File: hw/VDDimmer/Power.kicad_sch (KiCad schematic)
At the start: 37 parts, among them J2 VIN 9-24V, Q5 SUD50P06-15, U2 AP64350SP-13, U3 AMS1117-3.3

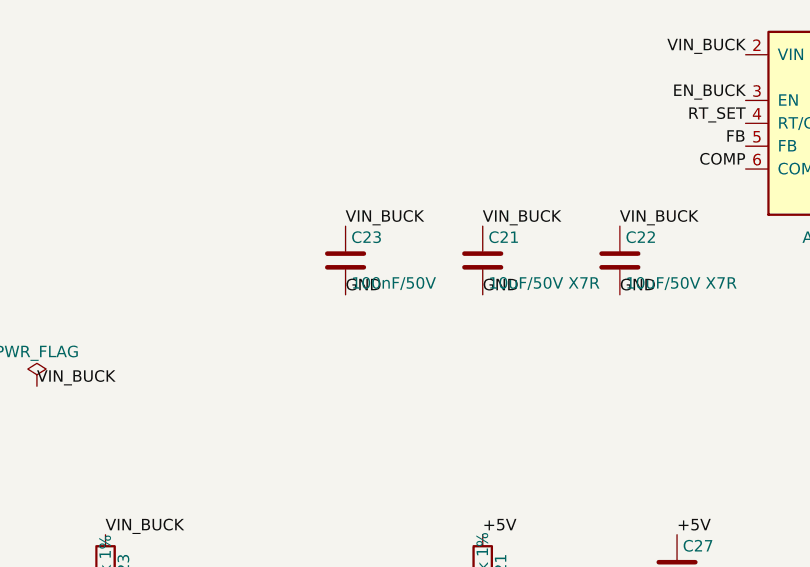
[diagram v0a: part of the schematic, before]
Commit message: Route input protection chain and VIN_BUCK distribution
C23 -> 0402 (100nF/25V): hot loop 14.31 -> 13.31 mm2, 11% margin.
VIN corridor necked to 0.6mm to hold clearance to the GND return.

Routed: VIN_RAW (J2->F1), VIN_FUSED (F1->D5->Q5 tab, routed above D5
to clear its GND pad), QREV_G (Q5 gate -> R20 -> D6), VIN_BUCK
distribution (R30/L3 -> C21/C22 -> R31 -> R23 -> buck), VIN_DAMP.

0 real DRC errors. 24-28 reported errors are C23's 4 phantom pads,
re-injected by update_pcb_from_schematic; place_component does not
have this bug but produces footprints with no schematic identity,
so it cannot carry nets.

Co-Authored-By: Claude Opus 5 (1M context) <noreply@anthropic.com>
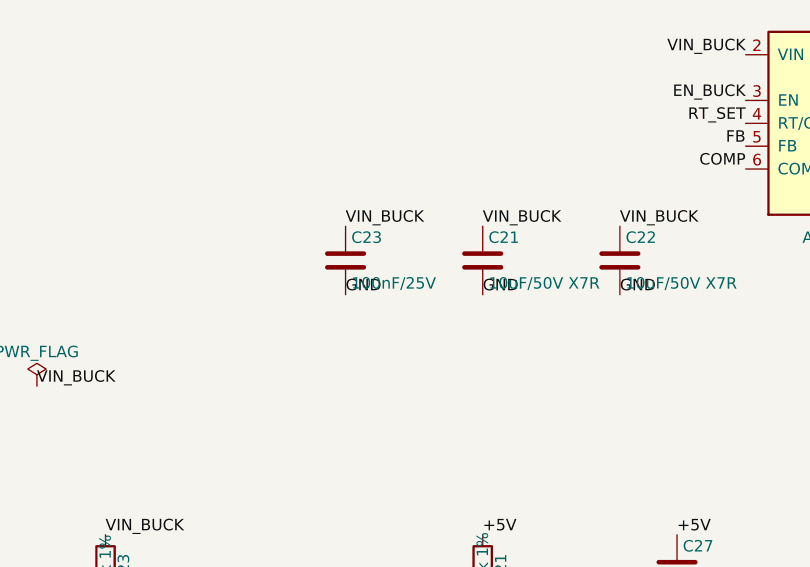
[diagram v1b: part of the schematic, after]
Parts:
- C23: value 100nF/50V -> 100nF/25V; footprint Capacitor_SMD:C_0603_1608Metric -> Capacitor_SMD:C_0402_1005Metric
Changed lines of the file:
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@@
 			)
 		)
-		(property "Value" "100nF/50V"
+		(property "Value" "100nF/25V"
 			(at 135.255 107.95 0)
 			(effects
@@
 			)
 		)
-		(property "Footprint" "Capacitor_SMD:C_0603_1608Metric"
+		(property "Footprint" "Capacitor_SMD:C_0402_1005Metric"
 			(at 134.62 105.41 0)
 			(hide yes)

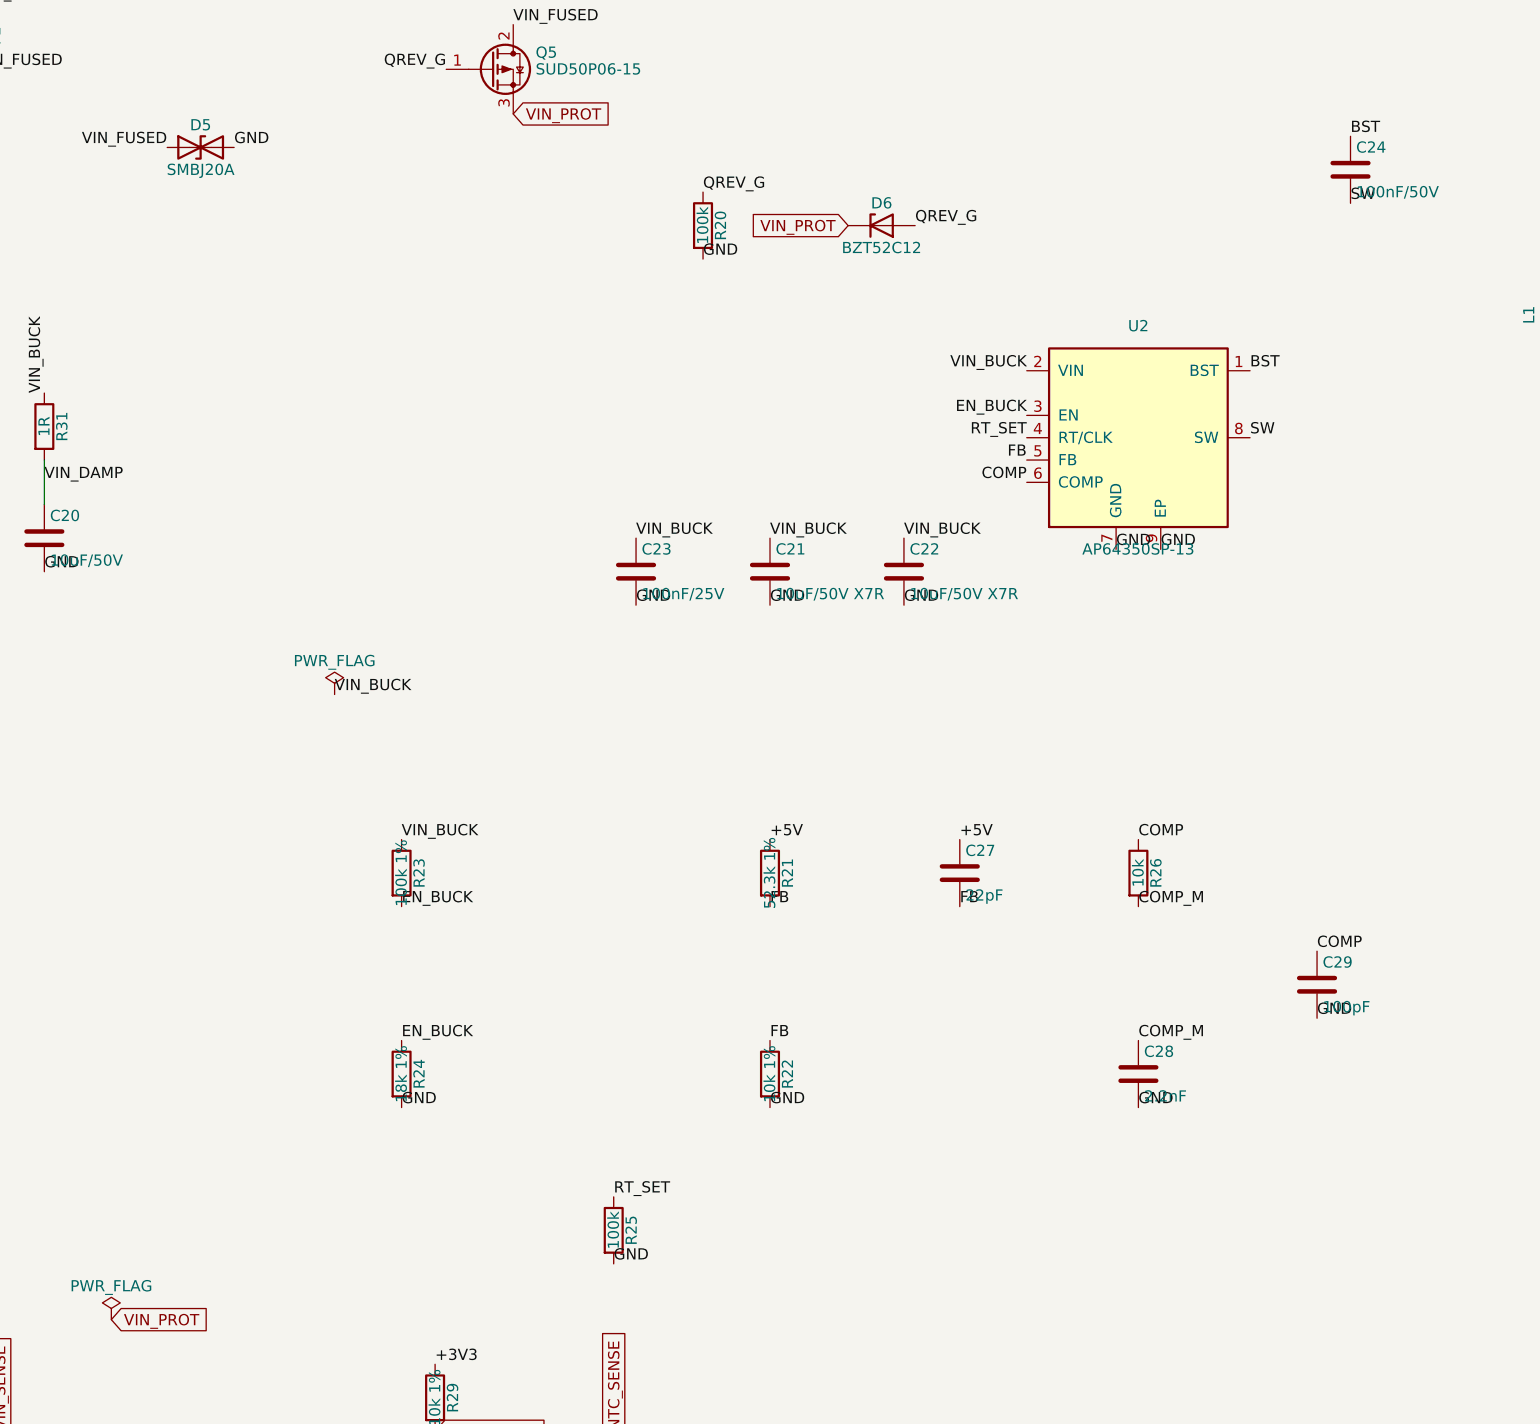
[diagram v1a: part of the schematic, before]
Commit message: Swap buck to AP63301WU-7: hot loop 13.31 -> 4.60 mm2
The AP64350's SO-8EP pinout (VIN pin2 / GND pin7 diagonal, BST and SW
between them) has no valid 2-layer routing: Cin above the IC forces a
VIN/BST crossing, Cin below encloses EN and RT with no escape that
doesn't either break the 8.5.3 keepout or push the hot loop to
16.5 mm2. Measured, not estimated.

AP63301WU-7 (C2158003, TSOT-23-6, 3.8-32V, 3A, 500kHz, spread
spectrum) has VIN (pin3) and GND (pin4) adjacent on the bottom edge.
Cin bridges them directly from below:

  hot loop  4.60 mm2  (target <15, 69% margin)
  vias in loop 0
  BST cap bridges pin6/pin5, adjacent on the right edge
  FB and EN on the free left edge, nothing enclosing them

Internally compensated at fixed 500kHz, so R25 (RT_SET), R26/C28
(COMP network) and C29 are deleted - 4 fewer parts and 3 fewer nets.
500kHz unchanged so L1 stays 10uH and C25/C26 unchanged. FB divider
unchanged: 52.3k/10k with 0.8V ref = 4.98V.

D5 SMBJ20A -> SMBJ18A (C19077573, Preferred, 42k stock): 29.2V clamp
sits under the AP63301's 32V abs max; SMBJ20A's 32.4V did not.

New symbol VANDIMMER:AP63301 authored. ERC 0/0, DRC 0 real errors.
Remaining 540 DRC errors are 24 Konnect phantom pads on U2 and C23.

Co-Authored-By: Claude Opus 5 (1M context) <noreply@anthropic.com>
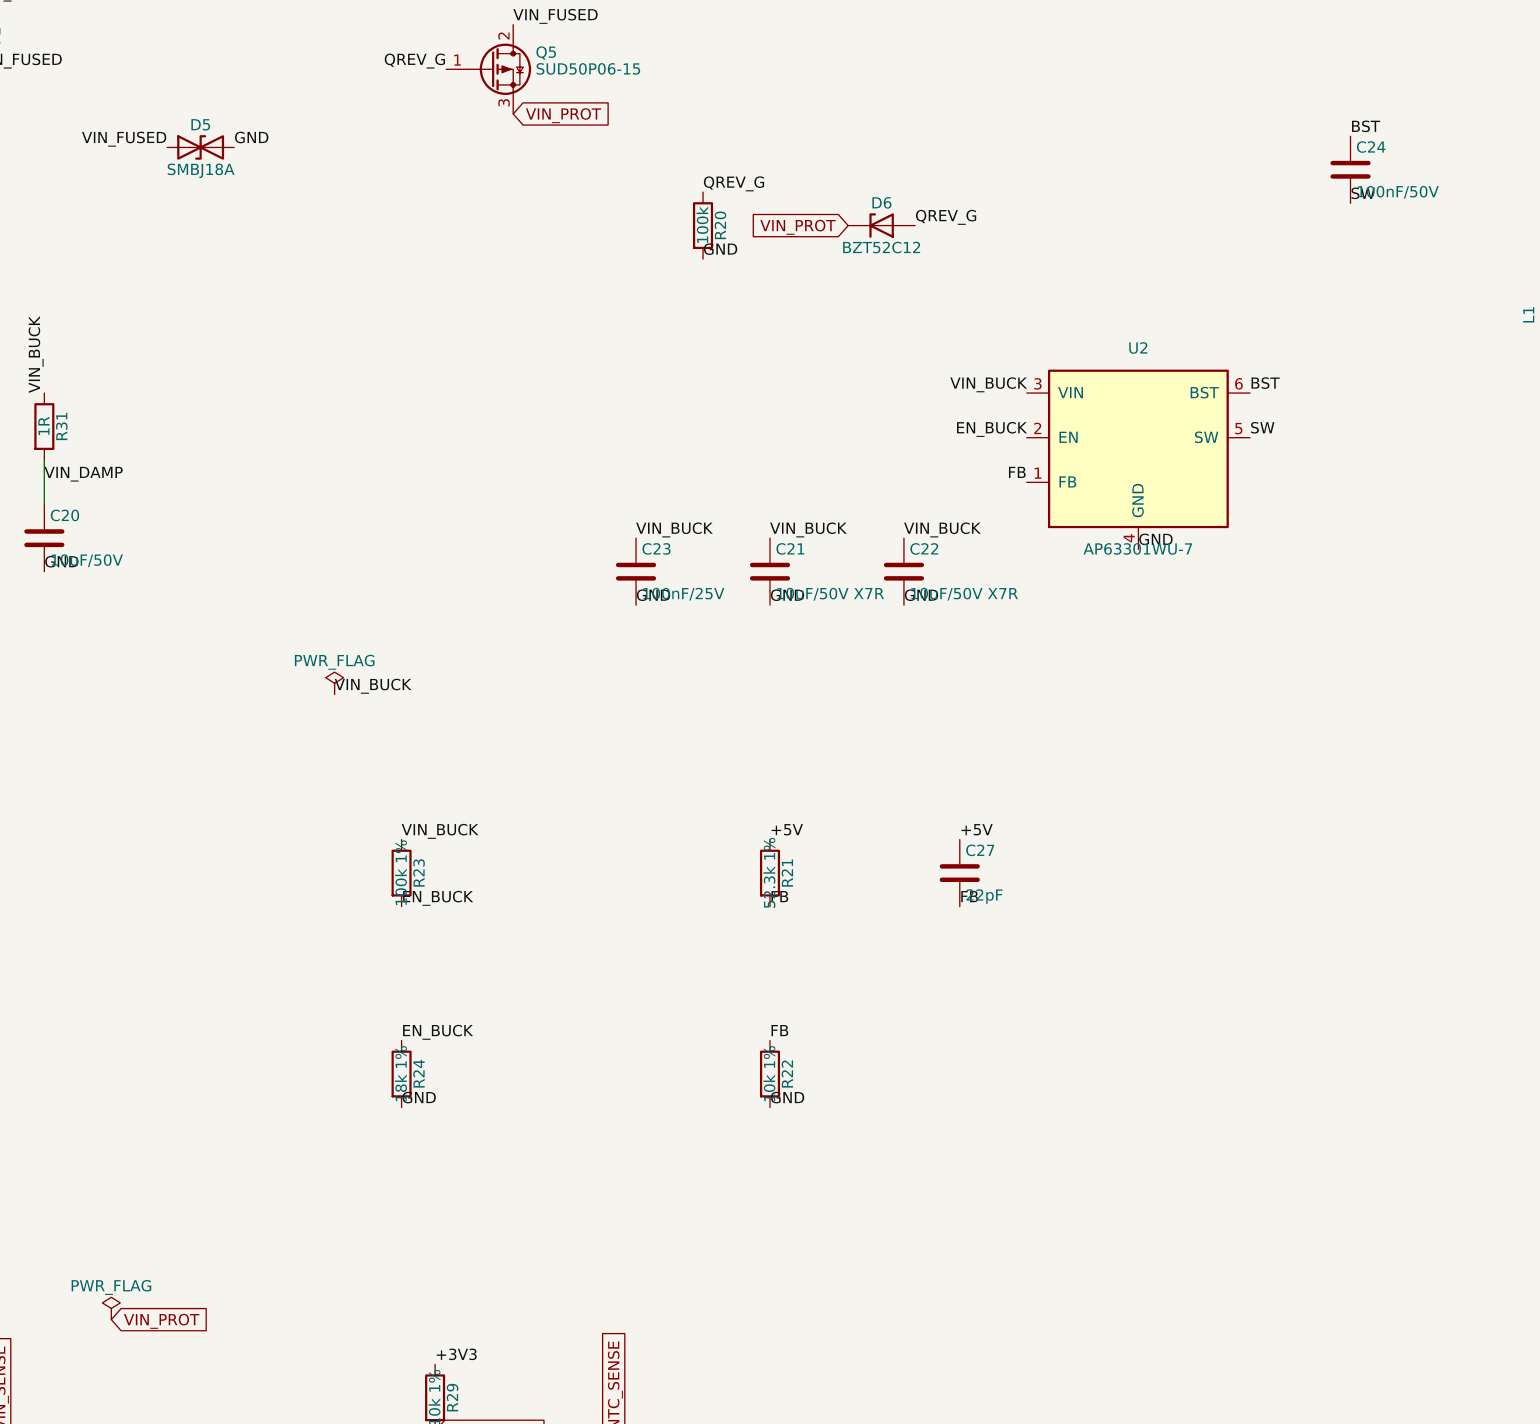
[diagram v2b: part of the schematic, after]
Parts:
- removed C28: 2.2nF, Capacitor_SMD:C_0603_1608Metric, symbol Device:C
- removed C29: 100pF, Capacitor_SMD:C_0603_1608Metric, symbol Device:C
- removed R25: 100k, Resistor_SMD:R_0805_2012Metric, symbol Device:R
- removed R26: 10k, Resistor_SMD:R_0805_2012Metric, symbol Device:R
- removed U2: AP64350SP-13, Package_SO:SOIC-8-1EP_3.9x4.9mm_P1.27mm_EP2.41x3.3mm_ThermalVias, symbol VANDIMMER:AP64350
- added U2: AP63301WU-7, Package_TO_SOT_SMD:TSOT-23-6, symbol VANDIMMER:AP63301
- D5: value SMBJ20A -> SMBJ18A
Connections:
- net BST: now also U2.6 (BST)
- net EN_BUCK: now also U2.2 (EN)
- net FB: now also U2.1 (FB)
- net GND: now also U2.4 (GND)
- net SW: now also U2.5 (SW)
- net VIN_BUCK: now also U2.3 (VIN)

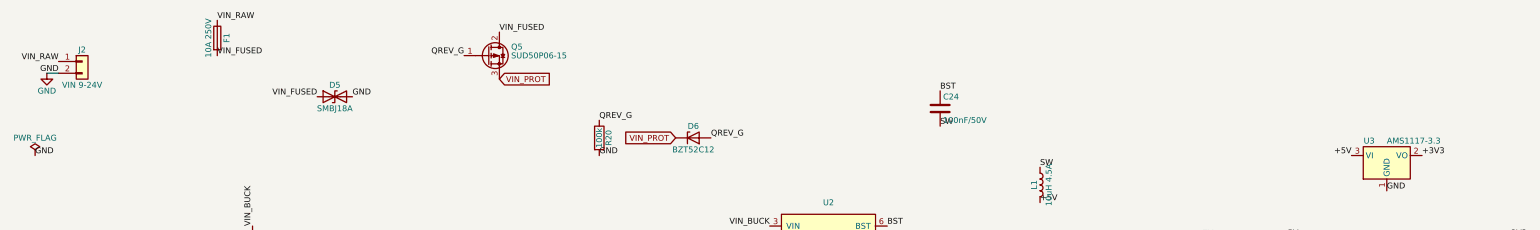
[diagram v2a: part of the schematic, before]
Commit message: Schematic pass: MPN/LCSC/Manufacturer on all 79 sourced parts
F1 -> "8A 250V", U3 -> "BL1117-33CX", J2 -> "VIN 12V" (was "VIN 9-24V",
which invited 24 V into an 18 V TVS). R11/R12 values cleaned to "47R" with
the DNP intent moved into the Assembly field. ERC still 0 violations.

Every sourced part now carries MPN, LCSC and Manufacturer, plus an Assembly
note anywhere the choice needs explaining - why D5 is an SMBJ18A, why R30's
current rating still needs checking, why L1 is candidate-only.

Two things this pass could NOT do, both because no MCP tool writes them:

- KiCad's (dnp yes) attribute. R11 and R12 must be flagged in the GUI; their
  Assembly fields say so. All five text-only DNPs were in this state, but
  L3/C20/R31 are now fitted by decision, so only R11/R12 remain.
- Fields on units 2-5 of a multi-unit symbol. Konnect writes unit 1 only,
  where the GUI propagates to all units. U4/U5 are 5-unit 74HCT125s, so
  grouping a BOM by MPN splits U5 into two lines and would order 3 of a
  2-off part. tools/export-bom.sh groups by Value+Footprint instead, which
  collapses correctly - 49 lines, 96 parts, and the 15 lines without an LCSC
  are exactly the mounting holes and hand-fit connectors.

Also checked and left alone: the U4/U5 symbol's lib_id is 74AHCT125 while its
value is 74HCT125. AHCT would be the conventional WS2812 level shifter, but
JLC has 70 of it in SO-14 against 88,003 of the HCT part, and HCT is fine here
- TTL inputs, 15 ns against 300 ns bit times. The value is the buyable intent.

Co-Authored-By: Claude Opus 5 (1M context) <noreply@anthropic.com>
Claude-Session: https://claude.ai/code/session_01QsYnM2qRBWQsyKPH1v7rLR
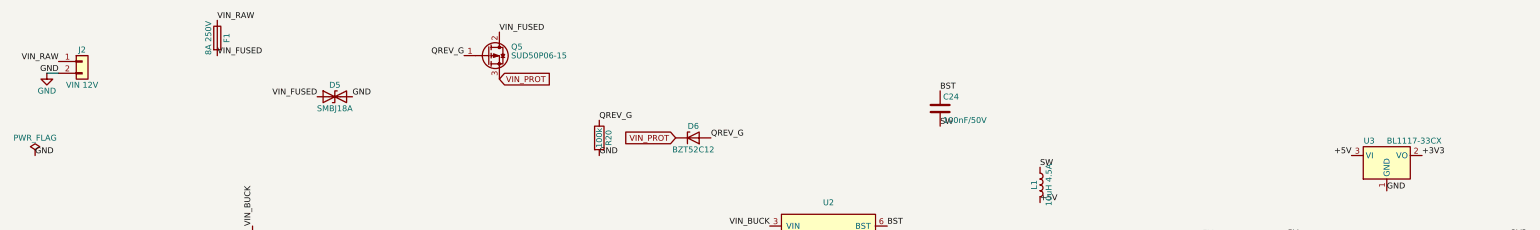
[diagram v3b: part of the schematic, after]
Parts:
- C20: Assembly DNP - spare input cap, populate with L3 -> LC filter cap - NOW FITTED per the 2026-08-29 decision, no 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; LCSC (none) -> C5156756; MPN (none) -> FS32X106K101EGG; Manufacturer (none) -> PSA
- C21, C22: LCSC (none) -> C5156756; MPN (none) -> FS32X106K101EGG; Manufacturer (none) -> PSA
- C23: Assembly (none) -> buck Cin - keep the 2.51 mm2 hot loop; do not relocate; LCSC (none) -> C307331; MPN (none) -> CL05B104KB54PNC; Manufacturer (none) -> Samsung Electro-Mechanics
- C24, C32, C33, C34: LCSC (none) -> C14663; MPN (none) -> CC0603KRX7R9BB104; Manufacturer (none) -> YAGEO
- C25, C26, C31: LCSC (none) -> C12891; MPN (none) -> CL31A226KAHNNNE; Manufacturer (none) -> Samsung Electro-Mechanics
- C27: LCSC (none) -> C1653; MPN (none) -> CL10C220JB8NNNC; Manufacturer (none) -> Samsung Electro-Mechanics
- C30: LCSC (none) -> C15850; MPN (none) -> CL21A106KAYNNNE; Manufacturer (none) -> Samsung Electro-Mechanics
- D5: Assembly (none) -> 18 V standoff, 29.2 V clamp - under U2's 32 V abs max. The 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; LCSC (none) -> C19077573; MPN (none) -> SMBJ18A; Manufacturer (none) -> hongjiacheng
- D6: LCSC (none) -> C19077410; MPN (none) -> BZT52C12; Manufacturer (none) -> hongjiacheng
- F1: value 10A 250V -> 8A 250V; Assembly (none) -> 8 A fuse - sized for the 5 A board cap with 25% continuous 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; LCSC (none) -> C54824501; MPN (none) -> LTC2410-1800TSK; Manufacturer (none) -> LUTE
- J2: value VIN 9-24V -> VIN 12V; Assembly (none) -> hand-fit. 12 V ONLY - D5 is an SMBJ18A (18 V standoff); 24 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; MPN (none) -> MC 1,5/2-G-5.08; Manufacturer (none) -> Phoenix Contact
- L1: Assembly (none) -> CANDIDATE ONLY - verify land pattern. Board land is two 2.5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; LCSC (none) -> C2849537; MPN (none) -> PNLS6045-100M; Manufacturer (none) -> DMBJ
- L3: Assembly DNP - optional input LC filter, populate only if EMI sweep 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 -> NOW FITTED per the 2026-08-29 decision, no longer DNP. Same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; LCSC (none) -> C2849537; MPN (none) -> PNLS6045-100M; Manufacturer (none) -> DMBJ
- Q5: Assembly (none) -> 12 mOhm beats the spec's 30 mOhm assumption - reverse-polar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; LCSC (none) -> C7503186; MPN (none) -> SUD50P06-15(UMW); Manufacturer (none) -> UMW
- R20: LCSC (none) -> C149504; MPN (none) -> 0805W8F1003T5E; Manufacturer (none) -> UNI-ROYAL
- R21: Assembly (none) -> buck FB divider - extended library, attracts a JLC setup fee; LCSC (none) -> C2933465; MPN (none) -> FRC0805F5232TS; Manufacturer (none) -> FOJAN
- R22, R28, R29: LCSC (none) -> C17414; MPN (none) -> 0805W8F1002T5E; Manufacturer (none) -> UNI-ROYAL
- R23: Assembly (none) -> EN_BUCK UVLO divider upper leg - with R24 18k the buck enab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; LCSC (none) -> C149504; MPN (none) -> 0805W8F1003T5E; Manufacturer (none) -> UNI-ROYAL
- R24: LCSC (none) -> C17506; MPN (none) -> 0805W8F1802T5E; Manufacturer (none) -> UNI-ROYAL
- R27: Assembly (none) -> VIN_SENSE divider upper leg - with R28 10k gives 0.0909 rat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; LCSC (none) -> C149504; MPN (none) -> 0805W8F1003T5E; Manufacturer (none) -> UNI-ROYAL
- R30: Assembly (none) -> 0 R jumper carrying ~1.2 A - confirm the part's current rat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; LCSC (none) -> C17477; MPN (none) -> 0805W8F0000T5E; Manufacturer (none) -> UNI-ROYAL
- R31: Assembly DNP - LC filter damping, populate with L3 and C20 -> LC filter damping - NOW FITTED per the 2026-08-29 decision,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; LCSC (none) -> C25271; MPN (none) -> 0805W8F100KT5E; Manufacturer (none) -> UNI-ROYAL
- RT1: Assembly (none) -> +/-1% on both R and B; LCSC (none) -> C49247662; MPN (none) -> HNTC0805-103F3950FB; Manufacturer (none) -> hongjiacheng
- U2: Assembly (none) -> 32 V abs max - this is why the board is 12 V only and D5 is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; LCSC (none) -> C2158003; MPN (none) -> AP63301WU-7; Manufacturer (none) -> Diodes Incorporated
- U3: value AMS1117-3.3 -> BL1117-33CX; Assembly (none) -> 2 mA quiescent vs the AMS1117's 5 mA. No SOT-223 LDO goes l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; LCSC (none) -> C5400; MPN (none) -> BL1117-33CX; Manufacturer (none) -> BL (Shanghai Belling)
